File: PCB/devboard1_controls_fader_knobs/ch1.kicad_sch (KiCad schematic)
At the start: 66 parts, among them J10 ADDRSEL_1, J11 ADDRSEL_2, J12 ADDRSEL_0, J13 ADDRSEL_1, J14 ADDRSEL_2, J15 ADDRSEL_0, J16 ADDRSEL_1, J17 ADDRSEL_2, J18 KNOB_LED_D1, J19 KNOB_LED_D1, J20 KNOB_LED_D1, J21 KNOB_LED_D1, J22 KNOB_LED_P1, J23 KNOB_LED_P1, J24 KNOB_LED_P1, J25 KNOB_LED_P1, J26 KNOB_LED_D1, J27 KNOB_LED_D1, J28 KNOB_LED_P1, J29 KNOB_LED_P1, J30 KNOB_LED_D1, J31 KNOB_LED_D1, J32 KNOB_LED_D1, J33 KNOB_LED_D1, J34 KNOB_LED_P1, J35 KNOB_LED_P1, J36 KNOB_LED_P1, J37 KNOB_LED_P1, J6 ADDRSEL_0, J7 ADDRSEL_1, J8 ADDRSEL_2, J9 ADDRSEL_0, SW10 KNOB_CTRL_4A, SW11 LINE, SW12 PHASE, SW13 COMP, SW14 SOLO, SW15 KNOB_INPUT, SW16 KNOB_PAN, SW17 HIZ, SW18 HPF, SW19 SEND, SW2 FN1, SW20 MUTE, SW21 KNOB_CTRL_1B, SW22 KNOB_CTRL_2B, SW23 KNOB_CTRL_3B, SW24 KNOB_CTRL_4B, SW25 INS, SW26 PRE, SW27 SEL, SW3 FN2, SW4 MIC, SW5 V48, SW6 EQ, SW7 KNOB_CTRL_1A, SW8 KNOB_CTRL_2A, SW9 KNOB_CTRL_3A, U10 TTP223-BA6, U4 MCP23017x-x-ML, U5 MCP23017x-x-ML, U6 MCP23017x-x-ML, U7 MCP23017x-x-ML, U8 74HCT595, U9 74HCT595

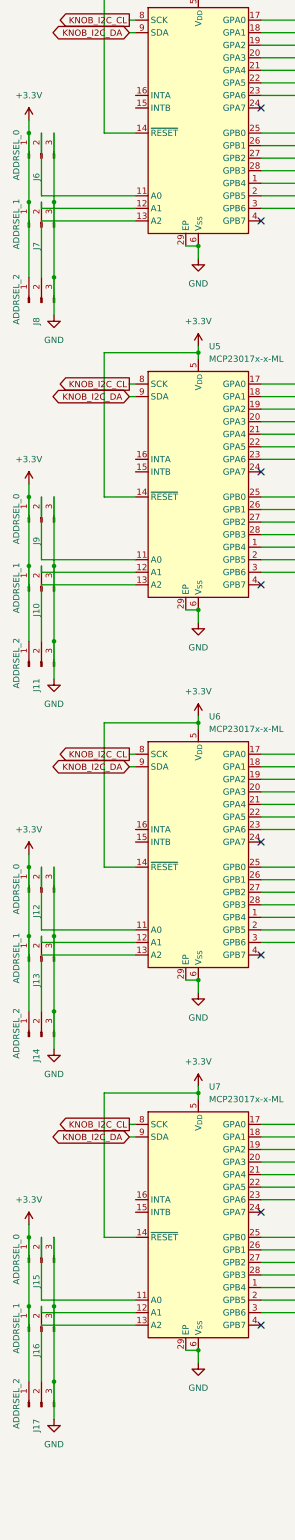
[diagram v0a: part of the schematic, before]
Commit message: led ring redesign
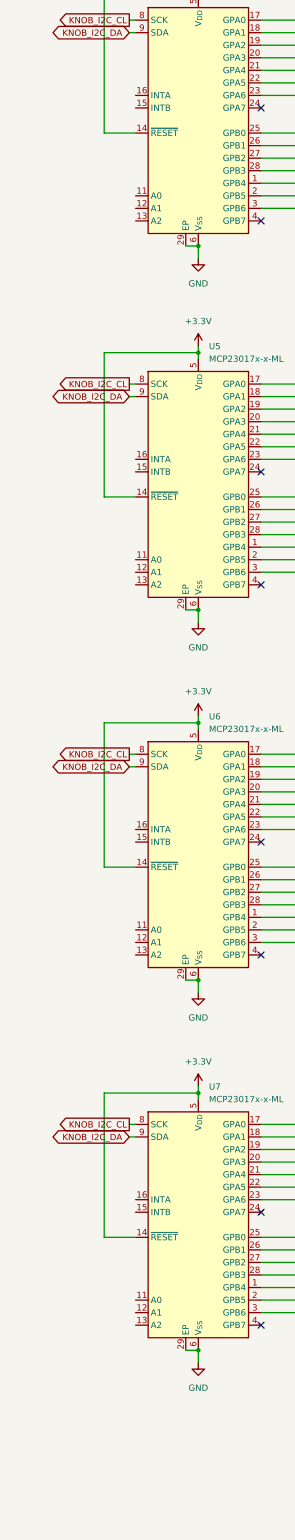
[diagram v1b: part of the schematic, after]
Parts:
- removed J10, J13, J16, J7: ADDRSEL_1, Connector_PinHeader_2.54mm:PinHeader_1x03_P2.54mm_Vertical, symbol Connector:Conn_01x03_Pin
- removed J11, J14, J17, J8: ADDRSEL_2, Connector_PinHeader_2.54mm:PinHeader_1x03_P2.54mm_Vertical, symbol Connector:Conn_01x03_Pin
- removed J12, J15, J6, J9: ADDRSEL_0, Connector_PinHeader_2.54mm:PinHeader_1x03_P2.54mm_Vertical, symbol Connector:Conn_01x03_Pin
